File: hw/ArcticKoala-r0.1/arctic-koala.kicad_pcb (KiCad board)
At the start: 4 copper layers, 50 x 37 mm, 97 parts, among them J1 Jumper, J14 PMOD, J18 Jumper, J2 Jumper, J20 Flash, J21 PMOD, J22 PMOD, J23 PMOD, J26 5V AUX, J27 5V AUX, J28 CRESET, J29 Jumper, P1 pkl_USB_OTG, P2 UP, P3 UP, P4 UP, P5 UP, SW1 TACT, U1 93C46B-SOT-23-6, U2 PSRAM, U4 FT2232H, U5 W25Q128JV-DTR, U6 LIFCL40-NX, U7 12MHz

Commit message: Updated KiCad files
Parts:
- removed J14: PMOD, Connector_PinSocket_2.54mm:PinSocket_2x06_P2.54mm_Vertical
- added J3: Conn_02x07_Odd_Even, Connector_PinSocket_2.54mm:PinSocket_2x07_P2.54mm_Vertical, B.Cu at (52.6, 61.5)
- moved J20 1.27 mm to (56.4, 64.0)
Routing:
- net +1V8: track 94.6 -> 107.8 mm, vias 9 -> 10
- net /CK_P: track 16.0 -> 20.4 mm
- net /D0P: track 19.1 -> 16.2 mm
- net /CK_N: track 19.0 -> 21.9 mm
- net /D2P: track 20.1 -> 17.2 mm
- net /D2N: track 22.9 -> 20.0 mm
- net /D3P: track 25.8 -> 23.3 mm
- net /D3N: track 27.9 -> 25.4 mm
- net GND: track 31.5 -> 34.0 mm
- net /D1N: track 22.6 -> 20.5 mm
- net /D1P: track 20.5 -> 18.4 mm
- net /iCE_CDONE: track 27.0 -> 25.4 mm
- net /FLASH_~HLD~|~RST~|IO3: track 64.2 -> 62.7 mm
- net /FLASH_MISO|IO1: track 73.4 -> 72.4 mm
- net /FLASH_MOSI|IO0: track 53.6 -> 54.2 mm
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
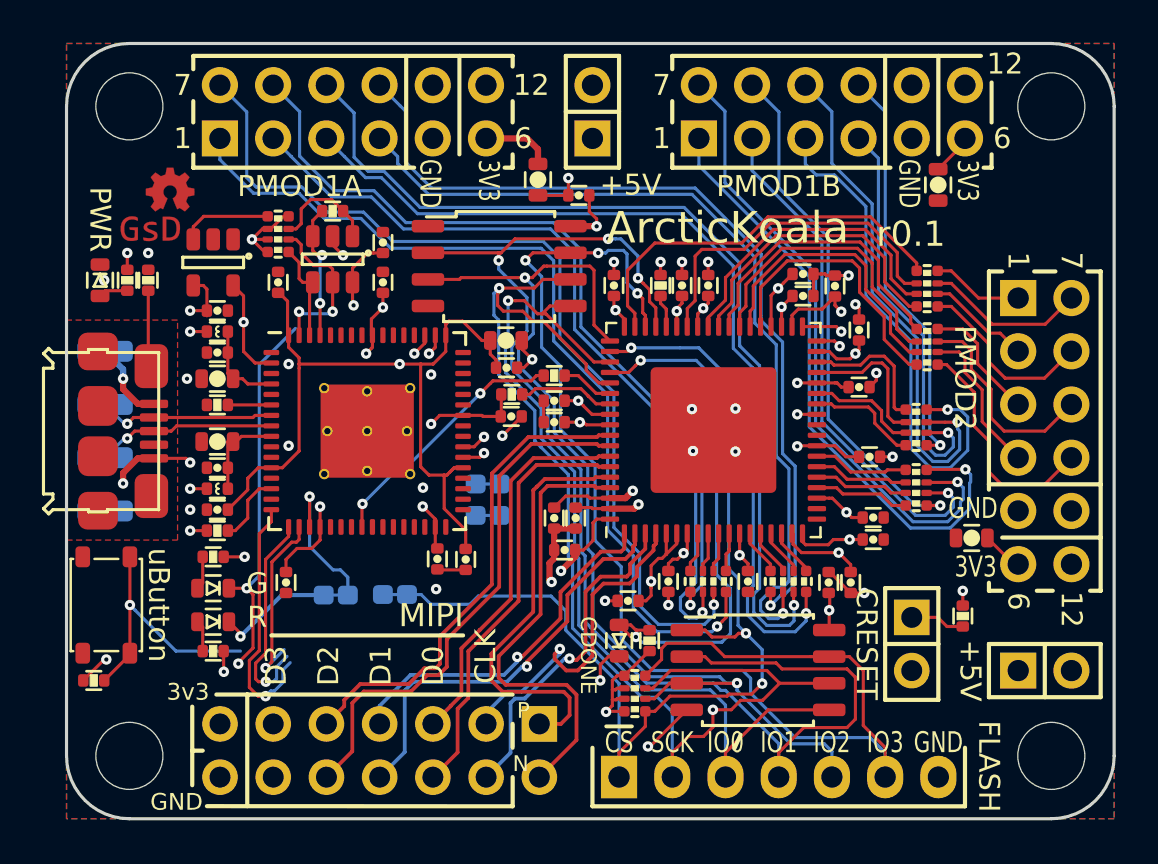
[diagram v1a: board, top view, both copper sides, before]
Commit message: Added ESD protection to MIPI lines
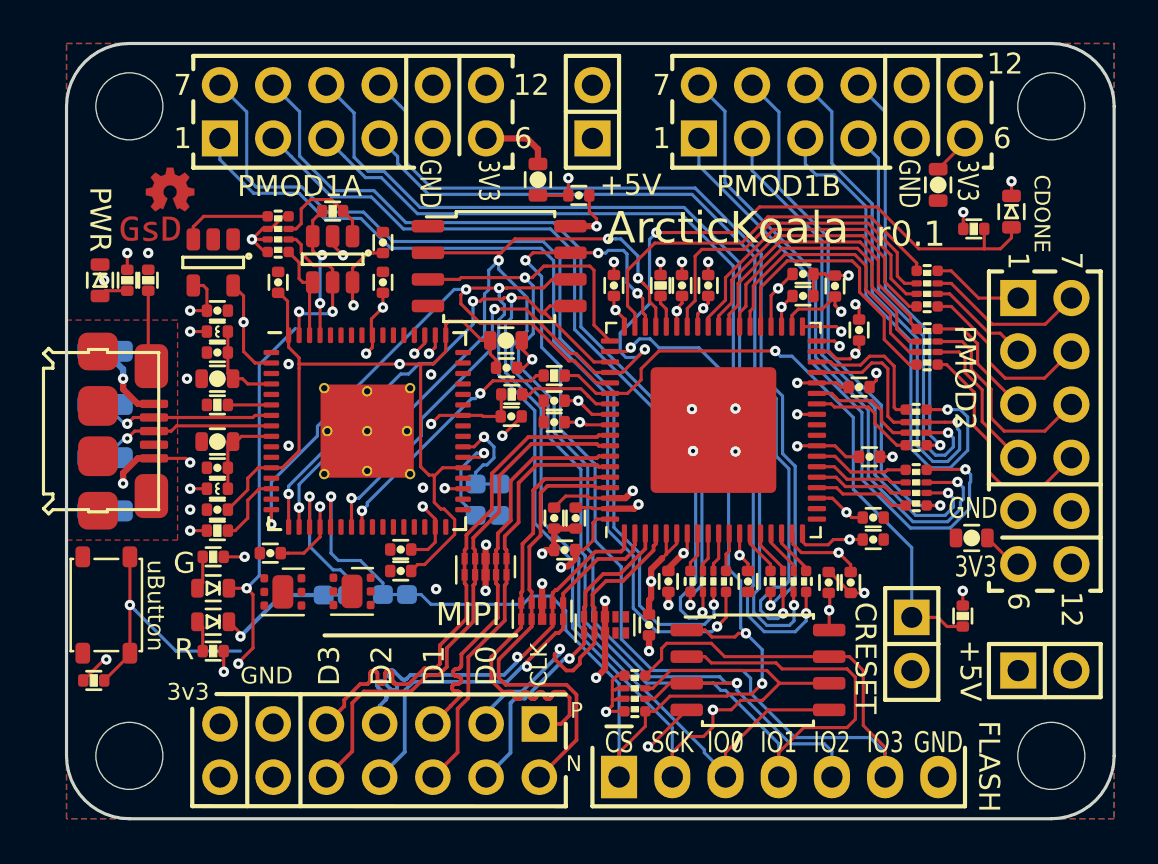
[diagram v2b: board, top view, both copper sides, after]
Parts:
- removed R12: 2k2, pkl_dipol:R_0402
- added R5: 4k7, pkl_dipol:R_0402, F.Cu at (73.3, 37.9)
- added REF**: WSON-6-1EP_2x2mm_P0.65mm_EP1x1.6mm, Package_SON:WSON-6-1EP_2x2mm_P0.65mm_EP1x1.6mm, F.Cu at (43.6, 55.1)
- added REF**: WSON-6-1EP_2x2mm_P0.65mm_EP1x1.6mm, Package_SON:WSON-6-1EP_2x2mm_P0.65mm_EP1x1.6mm, F.Cu at (40.3, 55.2)
- added U3: TPD4EUSB30, Package_SON:USON-10_2.5x1.0mm_P0.5mm, F.Cu at (50.0, 54.0)
- added U8: TPD4EUSB30, Package_SON:USON-10_2.5x1.0mm_P0.5mm, F.Cu at (52.7, 56.1)
- added U9: TPD4EUSB30, Package_SON:USON-10_2.5x1.0mm_P0.5mm, F.Cu at (55.7, 56.8)
- moved D3 27.7 mm to (75.1, 37.0), turned to 270 degrees
- moved C16 3.15 mm to (46.0, 54.2), turned to 180 degrees
- moved C19 1.81 mm to (46.0, 53.1), turned to 180 degrees
- moved C18 1.59 mm to (39.7, 53.3), turned to 180 degrees
- moved C3 1.52 mm to (57.8, 56.8), turned to 270 degrees
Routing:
- net /iCE_CRESET: track 5.13 -> 29.9 mm, vias 0 -> 1
- net /iCE_CDONE: track 25.4 -> 50.1 mm, vias 2 -> 4
- net /FLASH_MISO|IO1: track 72.4 -> 81.3 mm
- net /iCE_SS_B: track 0.00 -> 7.78 mm, vias 0 -> 1
- net /iCE_SCK: track 68.6 -> 75.4 mm, vias 3 -> 4
- net GND: track 34.0 -> 39.3 mm, vias 34 -> 40
- net /FLASH_MOSI|IO0: track 54.2 -> 59.2 mm, vias 2 -> 3
- net +1V0: track 76.0 -> 80.3 mm
- net /xFIFO_D0: track 1.08 -> 5.01 mm
- net /D2P: track 17.2 -> 20.2 mm
- net /xFIFO_D1: track 1.20 -> 4.11 mm
- net +3V3: track 65.0 -> 62.2 mm, vias 22 -> 23
- net +1V8: track 107.8 -> 110.0 mm
- net /D3P: track 23.3 -> 25.3 mm
- net /CK_P: track 20.4 -> 21.5 mm
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
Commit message: Completed hardware design files
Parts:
- removed D4: GRN, pkl_dipol:D_0603
- removed the REF** at (43.6, 55.1)
- removed the REF** at (40.3, 55.2)
- added C41: 22pF, pkl_dipol:C_0402, F.Cu at (34.8, 59.2)
- added C42: 4.7uF, pkl_dipol:C_0402, F.Cu at (36.6, 56.1)
- added C43: 4.7uF, pkl_dipol:C_0603, F.Cu at (36.4, 53.9)
- added C44: 100nF, pkl_dipol:C_0402, F.Cu at (41.6, 53.2)
- added C45: 22pF, pkl_dipol:C_0402, F.Cu at (43.0, 58.0)
- added C46: 4.7uF, pkl_dipol:C_0402, F.Cu at (40.2, 55.9)
- added C47: 100nF, pkl_dipol:C_0402, F.Cu at (40.2, 53.9)
- added C48: 4.7uF, pkl_dipol:C_0402, F.Cu at (43.7, 54.7)
- added C49: 4.7uF, pkl_dipol:C_0402, F.Cu at (40.6, 59.1)
- added C50: 4.7uF, pkl_dipol:C_0402, F.Cu at (47.5, 53.6)
- added L3: 1.0uH, Inductor_SMD:L_0603_1608Metric, F.Cu at (36.8, 57.8)
- added L4: 1.0uH, Inductor_SMD:L_0603_1608Metric, F.Cu at (45.7, 56.6)
- added L5: 1.0uH, Inductor_SMD:L_0603_1608Metric, F.Cu at (40.6, 57.8)
- added R12: R, pkl_dipol:R_0402, F.Cu at (36.6, 59.0)
- added R16: R, pkl_dipol:R_0402, F.Cu at (38.6, 59.0)
- added R17: R, pkl_dipol:R_0402, F.Cu at (45.2, 57.9)
- added R18: R, pkl_dipol:R_0402, F.Cu at (46.6, 58.4)
- added R19: R, pkl_dipol:R_0402, F.Cu at (42.5, 59.0)
- added R25: R, pkl_dipol:R_0402, F.Cu at (43.7, 56.6)
- added R27: 2k2, pkl_dipol:R_0402, F.Cu at (69.4, 54.0)
- added R28: 2k2, pkl_dipol:R_0402, F.Cu at (71.3, 54.0)
- added R29: 4k7, pkl_dipol:R_0402, F.Cu at (45.1, 36.8)
- added U10: TPS62067, Package_SON:WSON-8-1EP_2x2mm_P0.5mm_EP0.9x1.6mm_ThermalVias, F.Cu at (38.4, 55.4)
- added U11: TPS62067, Package_SON:WSON-8-1EP_2x2mm_P0.5mm_EP0.9x1.6mm_ThermalVias, F.Cu at (45.8, 54.3)
- added U12: TPS62067, Package_SON:WSON-8-1EP_2x2mm_P0.5mm_EP0.9x1.6mm_ThermalVias, F.Cu at (42.0, 55.4)
- C10: value 100n -> 4.7uF
- C7: value 4u7 -> 22pF; footprint pkl_dipol:C_0603 -> pkl_dipol:C_0402
- R14: value 330E -> 30R
- moved R14 31.6 mm to (68.5, 51.6)
- moved C7 16.8 mm to (45.2, 58.9)
- moved C16 12.2 mm to (51.0, 43.1), turned to 0 degrees
- moved C10 11.5 mm to (43.5, 53.2), turned to 180 degrees
- moved C19 10.3 mm to (51.0, 44.2), turned to 0 degrees
- moved R15 5.26 mm to (34.7, 53.3)
- moved J29 3.27 mm to (40.5, 53.0)
- moved J18 3.03 mm to (45.8, 52.3)
- moved D5 2.48 mm to (34.6, 55.8), turned to 90 degrees
- moved C18 1.58 mm to (38.1, 53.3)
- moved C5 1.24 mm to (67.8, 50.6)
- moved G*** 0.90 mm to (34.1, 35.8)
- moved C35 0.50 mm to (68.1, 48.3)
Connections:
- C10 pad 1: +1V8 -> +1V0
- C7 pad 1: +1V8 -> +1V0
- C7 pad 2: GND -> Net-(C7-Pad2)
- R13 pad 2: +3V3 -> +1V8
- R14 pad 1: Net-(D4-PadA) -> Net-(R14-Pad1)
- R14 pad 2: +3V3 -> /FTDI_CLK
- U4 pad 49: +1V8 -> Net-(U4-Pad49)
- U4 pad 50: +3V3 -> Net-(U4-Pad50)
- U6 pad 19: Net-(U6-Pad19) -> Net-(R14-Pad1)
- U6 pad 20: Net-(U6-Pad20) -> /PSRAM_CS
- U6 pad 27: Net-(U6-Pad27) -> /~BUTTON
- U6 pad 28: Net-(U6-Pad28) -> /~LEDR
- U6 pad 36: Net-(U6-Pad36) -> /Tx_TTL|FIFO_D1
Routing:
- net /~LEDR: track 5.72 -> 71.5 mm, vias 1 -> 4
- net /~BUTTON: track 12.6 -> 73.7 mm, vias 1 -> 4
- net /FTDI_CLK: track 4.91 -> 59.6 mm, vias 1 -> 4
- net /Tx_TTL|FIFO_D1: track 0.00 -> 48.8 mm, vias 0 -> 3
- net /PSRAM_CS: track 0.00 -> 37.8 mm, vias 0 -> 2
- net /Rx_TTL|FIFO_D0: track 0.00 -> 32.8 mm, vias 0 -> 3
- net +1V8: track 110.0 -> 141.2 mm, vias 10 -> 14
- net GND: track 39.3 -> 70.0 mm, vias 40 -> 48
- net +1V0: track 80.3 -> 100.1 mm, vias 10 -> 13
- net Net-(R27-Pad2): track 1.95 -> 20.6 mm, vias 1 -> 2
- net /~LEDG: track 18.2 -> 0.00 mm, vias 2 -> 0
- net +3V3: track 62.2 -> 75.6 mm, vias 23 -> 25
- net /FLASH_~HLD~|~RST~|IO3: track 62.7 -> 51.2 mm, vias 3 -> 4
- net +5V: track 115.7 -> 127.1 mm, vias 1 -> 2
- net Net-(C41-Pad2): track 0.00 -> 7.79 mm
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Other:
- board text added: "2"
- board text added: "3"
- board text removed: "D2"
- board text removed: "D3"
- board text removed: "R"
- board text removed: "uButton"

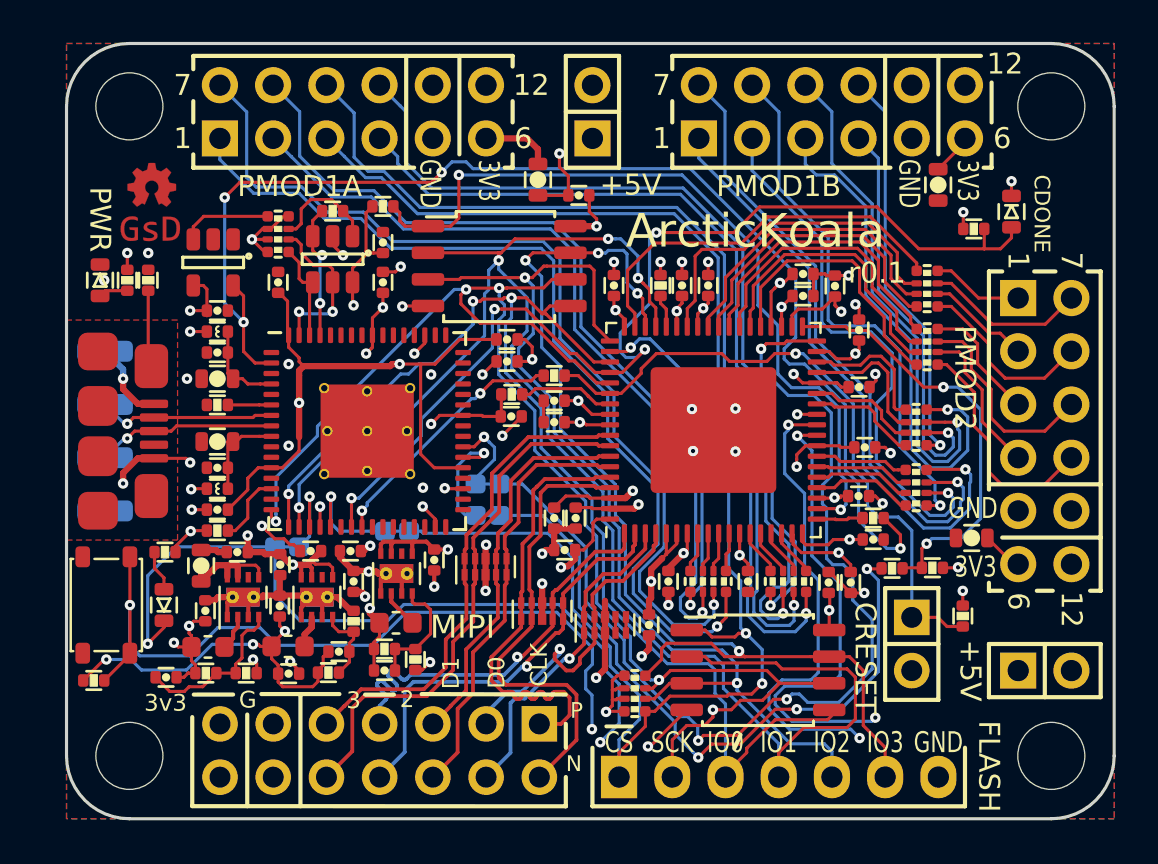
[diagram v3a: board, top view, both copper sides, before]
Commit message: Added logo to PCB, cleaned up Silkscreen
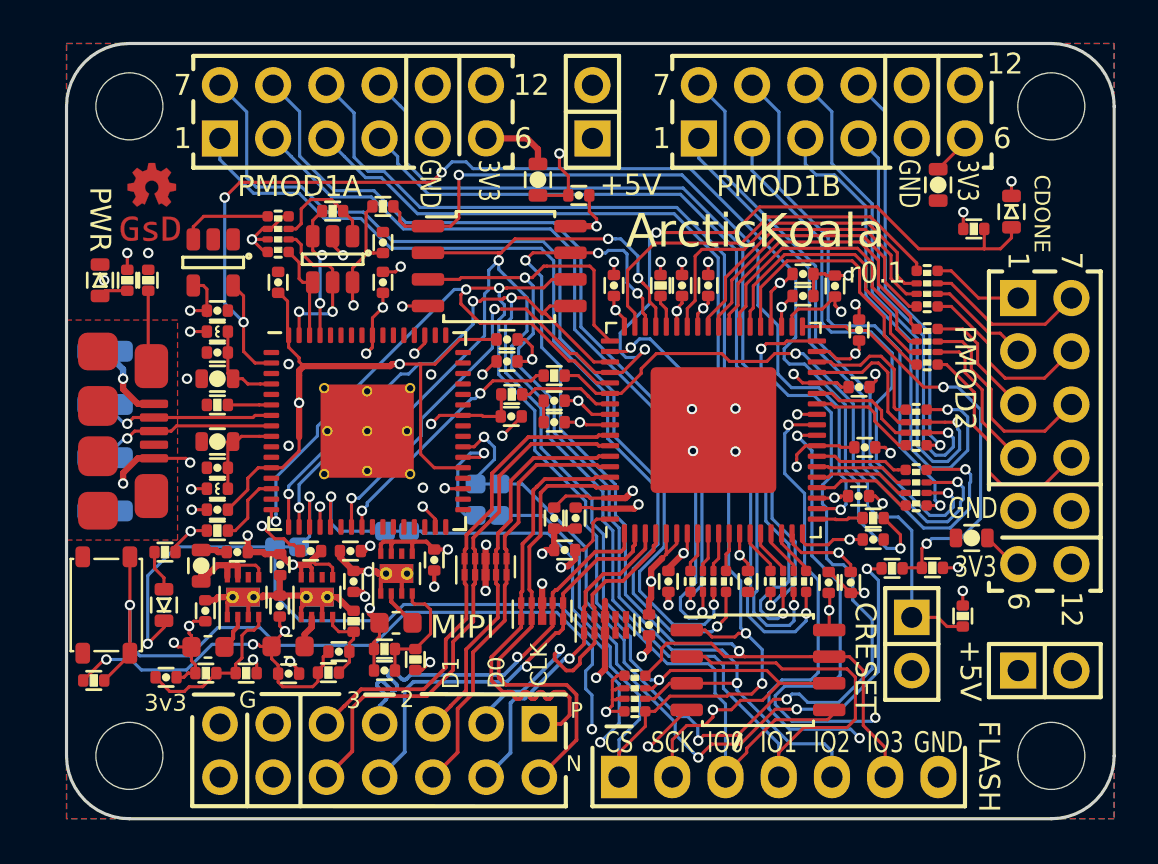
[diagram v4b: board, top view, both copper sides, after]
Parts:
- added G***: LOGO, Koala, B.Cu at (58.4, 45.7)
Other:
- board text added: "D2"
- board text added: "D3"
- board text added: "Rx"
- board text added: "Tx"
- board text added: "~SS"
- board text removed: "3V3 5V0"
- board text removed: "AUX CS"
- board text removed: "FPGA"
- board text removed: "GND GND"
- board text removed: "RGB0 RGB1"
- board text removed: "RGB2 1V2"
- board text removed: "RGBLED"

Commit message: hw: Add Gerbers, BOM
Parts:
- removed D3: BLU, pkl_dipol:D_0603
- removed the R5 at (32.9, 40.3)
- added D2: GREEN, pkl_dipol:D_0603, F.Cu at (31.6, 40.3)
- added R30: 330E, pkl_dipol:R_0402, F.Cu at (32.9, 40.3)
- C32, C33, C34: value DNP -> 10uF
- C43: value 4.7uF -> 10uF
- C44, C47: value 100nF -> 100n
- D1: value GRN -> BLUE
- R12: value R -> 450k
- R16: value R -> 100k
- R17: value R -> 120k
- R18, R25: value R -> 180k
- R19: value R -> 360k
- R5: value 4k7 -> 2k2
- moved D1 43.6 mm to (75.1, 37.0)
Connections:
- D1 pad A: Net-(D1-PadA) -> /iCE_CDONE
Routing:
- net Net-(D2-PadA): track 0.00 -> 1.40 mm
- net Net-(D1-PadA): track 1.40 -> 0.00 mm
